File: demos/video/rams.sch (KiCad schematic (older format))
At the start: 8 parts, among them U12 SIM4X32, U13 SIM4X32, U14 SIM4X32, U15 SIM4X32, U16 SIM4X32, U17 SIM4X32, U18 SIM4X32, U19 SIM4X32

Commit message: Pcbnew: Minor fix in hotkeys. Demos: add an example to use  a local fp-lib-table and local libs, and update schematics and boards.
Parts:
- U12, U13, U14, U15, U16, U17, U18, U19: footprint (none) -> footprints:sim72
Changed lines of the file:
@@
-EESchema Schematic File Version 2  date 18/11/2010 18:50:34
+EESchema Schematic File Version 2
 LIBS:power
 LIBS:device
@@
 LIBS:xilinx
 LIBS:special
-LIBS:microcontrollers
-LIBS:dsp
-LIBS:microchip
 LIBS:analog_switches
 LIBS:motorola
-LIBS:texas
 LIBS:intel
 LIBS:audio
 LIBS:interface
-LIBS:digital-audio
 LIBS:philips
-LIBS:display
 LIBS:cypress
 LIBS:siliconi
-LIBS:opto
-LIBS:atmel
-LIBS:contrib
-LIBS:valves
 LIBS:video-cache
-EELAYER 24  0
+EELAYER 24 0
 EELAYER END
-$Descr A3 16535 11700
+$Descr A3 16535 11693
+encoding utf-8
 Sheet 6 8
 Title "Kicad EDA"
@@
 F 0 "U13" H 10500 8050 70  0000 C CNN
 F 1 "SIM4X32" H 10950 5500 70  0000 C CNN
+F 2 "footprints:sim72" H 10500 7500 60  0001 C CNN
+F 3 "" H 10500 7500 60  0001 C CNN
 	1    10500 7500
 	1    0    0    -1
@@
 F 0 "U14" H 7700 8050 70  0000 C CNN
 F 1 "SIM4X32" H 8150 5500 70  0000 C CNN
+F 2 "footprints:sim72" H 7700 7500 60  0001 C CNN
+F 3 "" H 7700 7500 60  0001 C CNN
 	1    7700 7500
 	1    0    0    -1
@@
 F 0 "U12" H 4850 8050 70  0000 C CNN
 F 1 "SIM4X32" H 5300 5500 70  0000 C CNN
+F 2 "footprints:sim72" H 4850 7500 60  0001 C CNN
+F 3 "" H 4850 7500 60  0001 C CNN
 	1    4850 7500
 	1    0    0    -1
@@
 F 0 "U16" H 2000 8050 70  0000 C CNN
 F 1 "SIM4X32" H 2450 5500 70  0000 C CNN
+F 2 "footprints:sim72" H 2000 7500 60  0001 C CNN
+F 3 "" H 2000 7500 60  0001 C CNN
 	1    2000 7500
 	1    0    0    -1
@@
 F 0 "U15" H 10500 3600 70  0000 C CNN
 F 1 "SIM4X32" H 10950 1050 70  0000 C CNN
+F 2 "footprints:sim72" H 10500 3050 60  0001 C CNN
+F 3 "" H 10500 3050 60  0001 C CNN
 	1    10500 3050
 	1    0    0    -1
@@
 F 0 "U17" H 7700 3600 70  0000 C CNN
 F 1 "SIM4X32" H 8150 1050 70  0000 C CNN
+F 2 "footprints:sim72" H 7700 3050 60  0001 C CNN
+F 3 "" H 7700 3050 60  0001 C CNN
 	1    7700 3050
 	1    0    0    -1
@@
 F 0 "U18" H 4850 3600 70  0000 C CNN
 F 1 "SIM4X32" H 5300 1050 70  0000 C CNN
+F 2 "footprints:sim72" H 4850 3050 60  0001 C CNN
+F 3 "" H 4850 3050 60  0001 C CNN
 	1    4850 3050
 	1    0    0    -1
@@
 F 0 "U19" H 2000 3600 70  0000 C CNN
 F 1 "SIM4X32" H 2450 1050 70  0000 C CNN
+F 2 "footprints:sim72" H 2000 3050 60  0001 C CNN
+F 3 "" H 2000 3050 60  0001 C CNN
 	1    2000 3050
 	1    0    0    -1

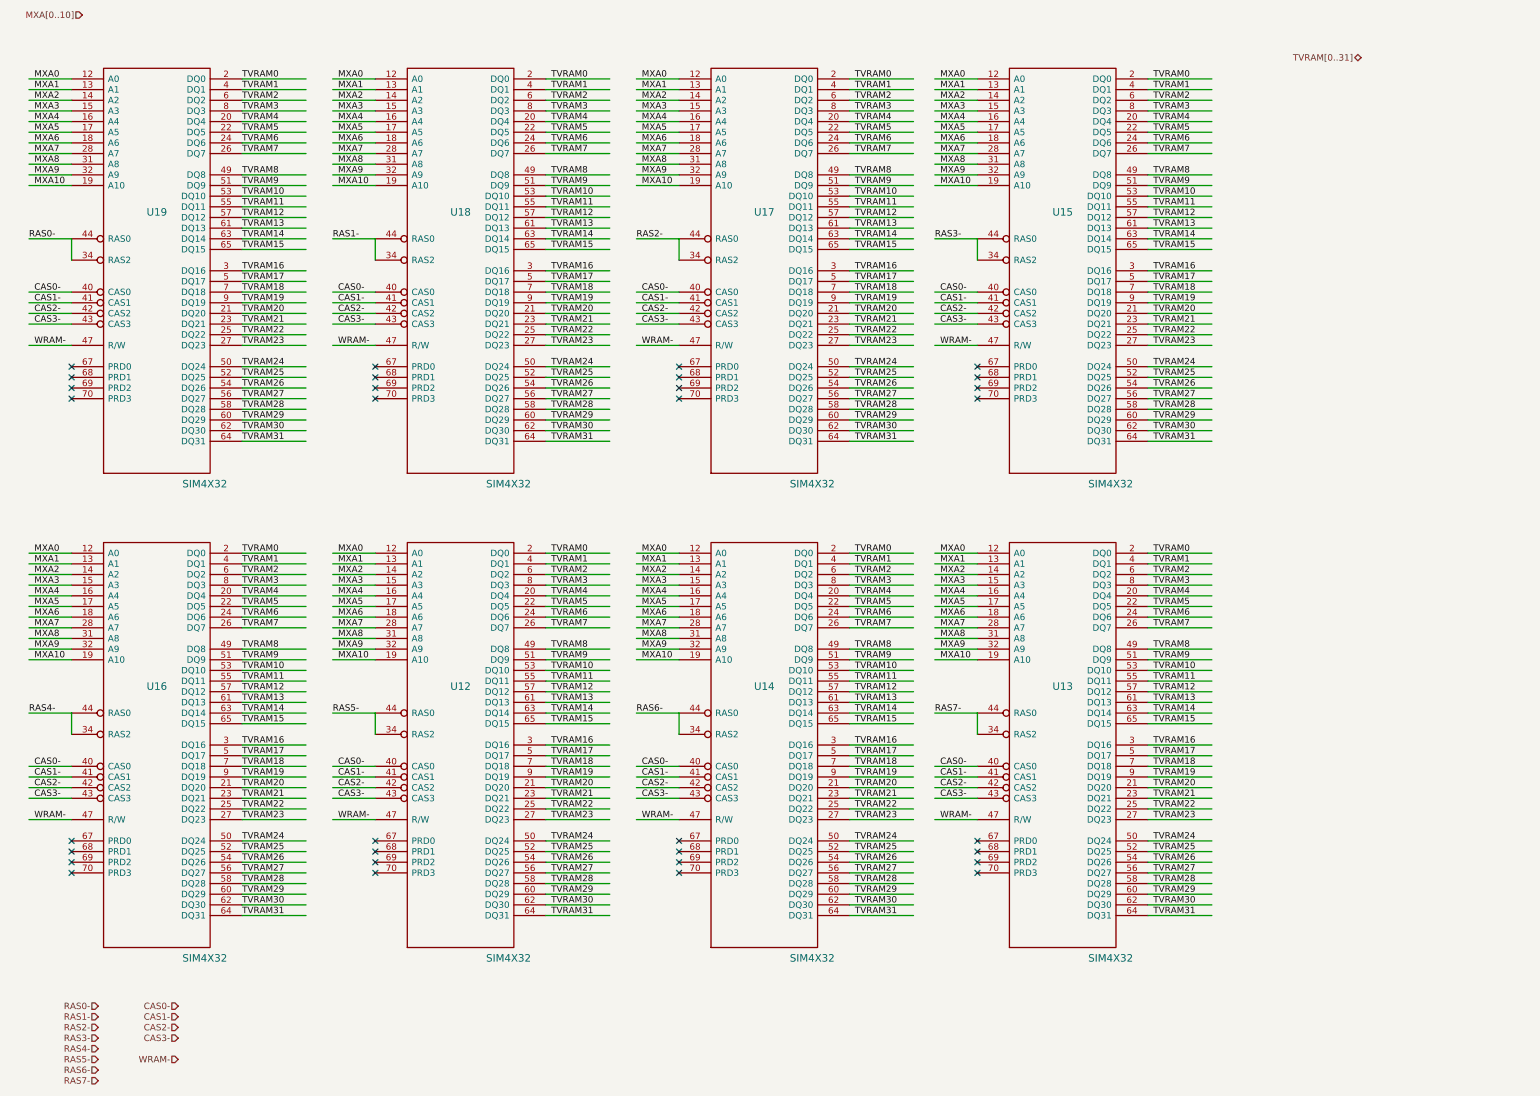
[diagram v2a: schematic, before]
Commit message: demos/ schematic tidying
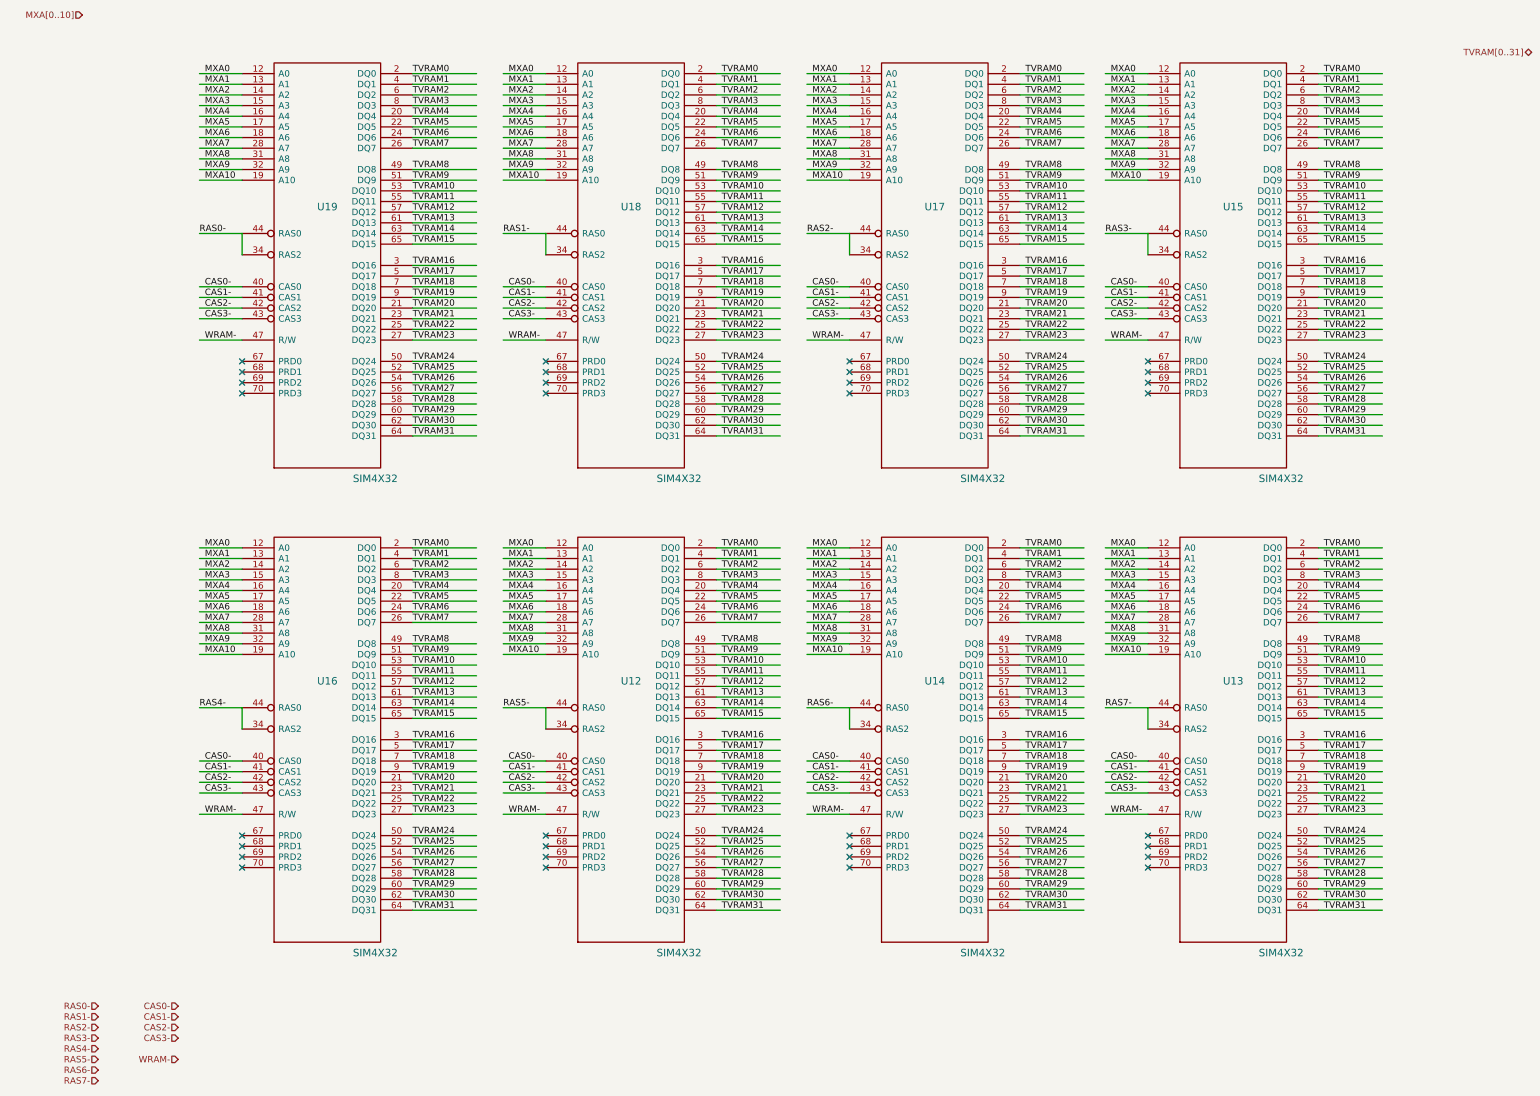
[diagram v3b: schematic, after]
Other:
- moved on the sheet: U12, U13, U14, U15, U16, U17, U18, U19
